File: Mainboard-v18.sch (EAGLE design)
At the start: 35 parts, among them T1 2N3904, T2 2N3904

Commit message: modified:   Mainboard-v18.brd 	modified:   Mainboard-v18.pdf 	modified:   Mainboard-v18.sch 	new file:   Mainboard-v18_top.pdf
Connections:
- new net N$3: U$34.1
- net GND: no longer U$34.1
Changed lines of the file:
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@@
 <part name="GND1" library="supply1" deviceset="GND" device=""/>
 <part name="GND2" library="supply1" deviceset="GND" device=""/>
-<part name="GND3" library="supply1" deviceset="GND" device=""/>
 <part name="GND4" library="supply1" deviceset="GND" device=""/>
 <part name="GND5" library="supply1" deviceset="GND" device=""/>
@@
 <instance part="GND1" gate="1" x="30.48" y="40.64"/>
 <instance part="GND2" gate="1" x="99.06" y="93.98"/>
-<instance part="GND3" gate="1" x="147.32" y="132.08"/>
 <instance part="GND4" gate="1" x="101.6" y="147.32"/>
 <instance part="GND5" gate="1" x="78.74" y="147.32"/>
@@
 </segment>
 <segment>
+<pinref part="T1" gate="G1" pin="E"/>
+<pinref part="GND4" gate="1" pin="GND"/>
+</segment>
+<segment>
+<pinref part="T2" gate="G1" pin="E"/>
+<pinref part="GND5" gate="1" pin="GND"/>
+</segment>
+<segment>
+<pinref part="U$31" gate="G$1" pin="1"/>
+<pinref part="GND6" gate="1" pin="GND"/>
+</segment>
+</net>
+<net name="N$3" class="0">
+<segment>
 <wire x1="170.18" y1="134.62" x2="147.32" y2="134.62" width="0.1524" layer="91"/>
 <label x="152.4" y="134.62" size="1.778" layer="95"/>
 <pinref part="U$34" gate="G$1" pin="1"/>
-<pinref part="GND3" gate="1" pin="GND"/>
-</segment>
-<segment>
-<pinref part="T1" gate="G1" pin="E"/>
-<pinref part="GND4" gate="1" pin="GND"/>
-</segment>
-<segment>
-<pinref part="T2" gate="G1" pin="E"/>
-<pinref part="GND5" gate="1" pin="GND"/>
-</segment>
-<segment>
-<pinref part="U$31" gate="G$1" pin="1"/>
-<pinref part="GND6" gate="1" pin="GND"/>
-</segment>
-</net>
+</segment>
+</net>

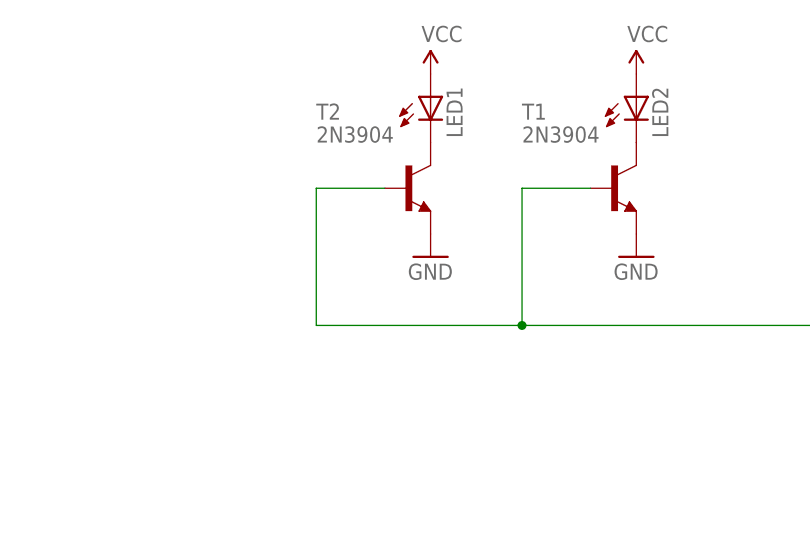
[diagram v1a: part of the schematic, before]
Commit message: modified:   Mainboard-v18.brd 	modified:   Mainboard-v18.sch
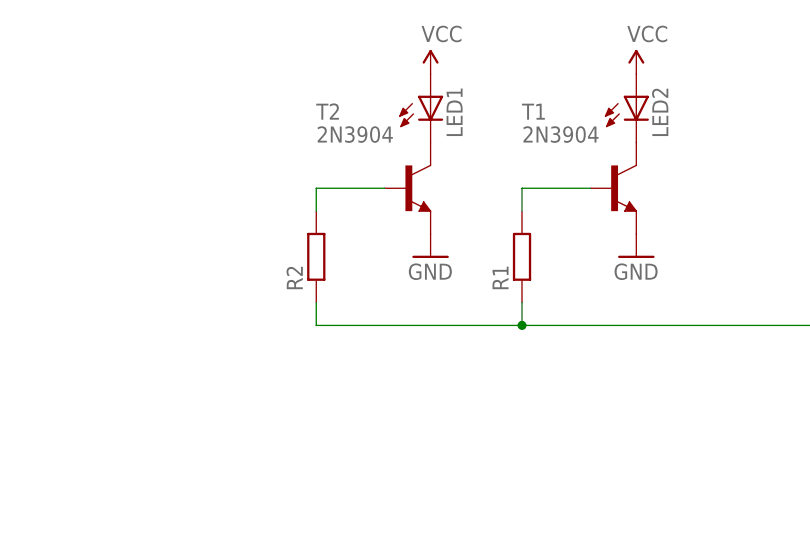
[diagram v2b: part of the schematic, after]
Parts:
- added R1, R2: (no value), resistor:R-EU_0204/5
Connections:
- new net N$4: R2.2, T2.B
- new net N$5: R1.2, T1.B
- net A3: now also R1.1, R2.1; no longer T1.B, T2.B
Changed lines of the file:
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@@
 <part name="PAD7" library="wirepad" deviceset="1,6/0,8" device=""/>
 <part name="PAD8" library="wirepad" deviceset="1,6/0,8" device=""/>
+<part name="R1" library="resistor" deviceset="R-EU_" device="0204/5"/>
+<part name="R2" library="resistor" deviceset="R-EU_" device="0204/5"/>
 </parts>
 <sheets>
@@
 <instance part="PAD7" gate="P" x="20.32" y="50.8"/>
 <instance part="PAD8" gate="P" x="20.32" y="43.18"/>
+<instance part="R1" gate="G$1" x="88.9" y="147.32" rot="R90"/>
+<instance part="R2" gate="G$1" x="66.04" y="147.32" rot="R90"/>
 </instances>
 <busses>
@@
 <pinref part="U$32" gate="G$1" pin="1"/>
 <wire x1="170.18" y1="139.7" x2="88.9" y2="139.7" width="0.1524" layer="91"/>
-<wire x1="88.9" y1="139.7" x2="88.9" y2="154.94" width="0.1524" layer="91"/>
-<pinref part="T1" gate="G1" pin="B"/>
-<wire x1="88.9" y1="154.94" x2="96.52" y2="154.94" width="0.1524" layer="91"/>
-<pinref part="T2" gate="G1" pin="B"/>
-<wire x1="73.66" y1="154.94" x2="66.04" y2="154.94" width="0.1524" layer="91"/>
-<wire x1="66.04" y1="154.94" x2="66.04" y2="139.7" width="0.1524" layer="91"/>
-<wire x1="66.04" y1="139.7" x2="88.9" y2="139.7" width="0.1524" layer="91"/>
+<pinref part="R2" gate="G$1" pin="1"/>
+<wire x1="88.9" y1="139.7" x2="66.04" y2="139.7" width="0.1524" layer="91"/>
+<wire x1="66.04" y1="142.24" x2="66.04" y2="139.7" width="0.1524" layer="91"/>
+<pinref part="R1" gate="G$1" pin="1"/>
+<wire x1="88.9" y1="142.24" x2="88.9" y2="139.7" width="0.1524" layer="91"/>
 <junction x="88.9" y="139.7"/>
 </segment>
@@
 </segment>
 </net>
+<net name="N$4" class="0">
+<segment>
+<pinref part="T2" gate="G1" pin="B"/>
+<wire x1="73.66" y1="154.94" x2="66.04" y2="154.94" width="0.1524" layer="91"/>
+<pinref part="R2" gate="G$1" pin="2"/>
+<wire x1="66.04" y1="152.4" x2="66.04" y2="154.94" width="0.1524" layer="91"/>
+</segment>
+</net>
+<net name="N$5" class="0">
+<segment>
+<pinref part="T1" gate="G1" pin="B"/>
+<wire x1="88.9" y1="154.94" x2="96.52" y2="154.94" width="0.1524" layer="91"/>
+<pinref part="R1" gate="G$1" pin="2"/>
+<wire x1="88.9" y1="152.4" x2="88.9" y2="154.94" width="0.1524" layer="91"/>
+</segment>
+</net>

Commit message: workaround
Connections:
- net GND: now also PAD2.P; no longer PAD3.P
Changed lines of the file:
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@@
-</segment>
-<segment>
-<pinref part="PAD3" gate="P" pin="P"/>
-<wire x1="99.06" y1="96.52" x2="88.9" y2="96.52" width="0.1524" layer="91"/>
-<pinref part="GND2" gate="1" pin="GND"/>
 </segment>
 <segment>
@@
 <pinref part="GND6" gate="1" pin="GND"/>
 </segment>
+<segment>
+<pinref part="PAD2" gate="P" pin="P"/>
+<pinref part="GND2" gate="1" pin="GND"/>
+<wire x1="88.9" y1="104.14" x2="99.06" y2="104.14" width="0.1524" layer="91"/>
+<wire x1="99.06" y1="104.14" x2="99.06" y2="96.52" width="0.1524" layer="91"/>
+</segment>
 </net>
